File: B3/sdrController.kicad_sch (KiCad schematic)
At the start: 5 parts, among them U314 74HC32, U316 74HC00, U317 74HC74, U318 74HC08, U319 74HC32

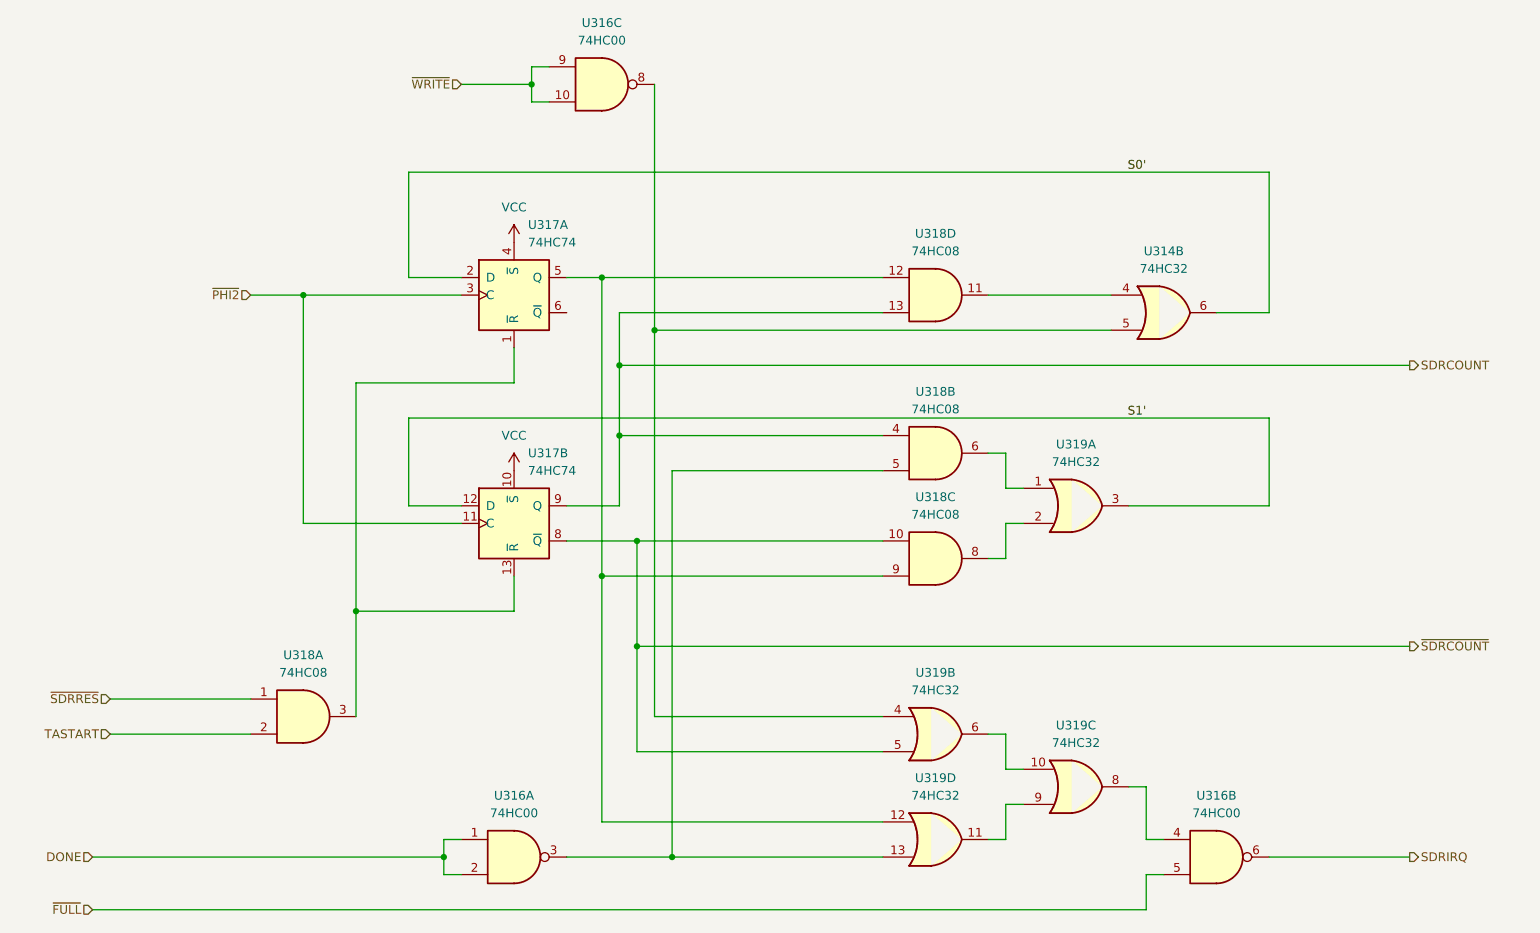
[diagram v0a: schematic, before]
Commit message: B3 added. First revision
Still not verified.
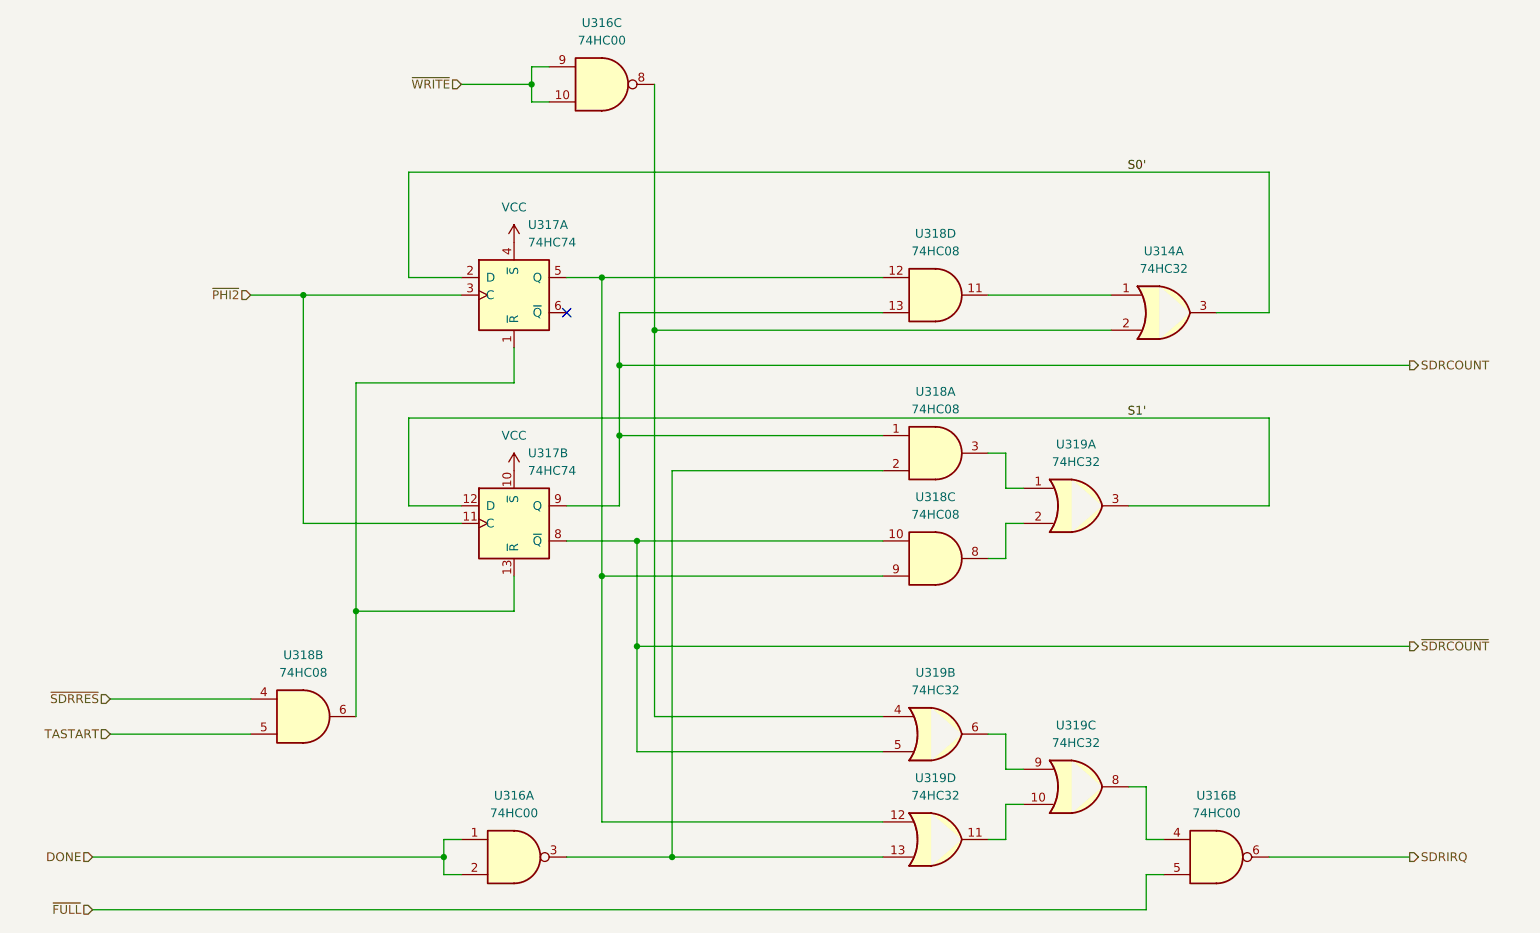
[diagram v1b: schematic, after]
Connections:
- net S0': now also U314.3; no longer U314.6
- net SDRCOUNT: now also U318.1; no longer U318.4
- net TASTART: now also U318.5; no longer U318.2
- net ~{SDRRES}: now also U318.4; no longer U318.1
- net at U318.11: now also U314.1; no longer U314.4
- net at U319.11: now also U319.10; no longer U319.9
- net at U316.3, U319.13: now also U318.2; no longer U318.5
- net at U316.8, U319.4: now also U314.2; no longer U314.5
- net at U319.6: now also U319.9; no longer U319.10
- net at U317.1 (~{R}), U317.13 (~{R}): now also U318.6; no longer U318.3
- net at U319.1: now also U318.3; no longer U318.6
- no-connect marks 0 -> 1
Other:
- moved on the sheet: U318A, U318B

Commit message: .
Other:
- company: (none) -> Daniel Molina
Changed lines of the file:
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@@
   (title_block
     (title "74HCT6526 Board 3")
-    (date "2022-09-11")
-    (rev "0.1")
+    (date "2022-10-08")
+    (rev "0.1.2")
+    (company "Daniel Molina")
+    (comment 1 "https://github.com/dmolinagarcia/74HCT6526")
   )
   (junction (at 127 68.58) (diameter 0) (color 0 0 0 0)

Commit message: .
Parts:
- added unit 4 of U316
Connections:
- net SDRIRQ: no longer names the net of U316.6
- net SDRIRQ: now also U316.12, U316.13
- new net ~{SDRIRQ}: U316.11
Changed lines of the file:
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@@
   (junction (at 127 68.58) (diameter 0) (color 0 0 0 0)
+  )
+  (junction (at 224.79 152.4) (diameter 0) (color 0 0 0 0)
   )
   (junction (at 137.16 152.4) (diameter 0) (color 0 0 0 0)
@@
     (stroke (width 0) (type default) (color 0 0 0 0))
   )
-  (wire (pts (xy 223.52 152.4) (xy 243.84 152.4))
-    (stroke (width 0) (type default) (color 0 0 0 0))
-  )
   (wire (pts (xy 182.88 109.22) (xy 185.42 109.22))
     (stroke (width 0) (type default) (color 0 0 0 0))
@@
     (stroke (width 0) (type default) (color 0 0 0 0))
   )
+  (wire (pts (xy 224.79 152.4) (xy 224.79 154.94))
+    (stroke (width 0) (type default) (color 0 0 0 0))
+  )
   (wire (pts (xy 91.44 116.84) (xy 114.3 116.84))
     (stroke (width 0) (type default) (color 0 0 0 0))
@@
     (stroke (width 0) (type default) (color 0 0 0 0))
   )
+  (wire (pts (xy 240.03 152.4) (xy 243.84 152.4))
+    (stroke (width 0) (type default) (color 0 0 0 0))
+  )
+  (wire (pts (xy 224.79 152.4) (xy 224.79 149.86))
+    (stroke (width 0) (type default) (color 0 0 0 0))
+  )
   (wire (pts (xy 116.84 40.64) (xy 116.84 38.1))
     (stroke (width 0) (type default) (color 0 0 0 0))
@@
   )
   (wire (pts (xy 83.82 71.12) (xy 106.68 71.12))
+    (stroke (width 0) (type default) (color 0 0 0 0))
+  )
+  (wire (pts (xy 223.52 152.4) (xy 224.79 152.4))
     (stroke (width 0) (type default) (color 0 0 0 0))
   )
@@
     (effects (font (size 1.27 1.27)) (justify right))
   )
-  (hierarchical_label "SDRIRQ" (shape output) (at 243.84 152.4 0)
+  (hierarchical_label "~{SDRIRQ}" (shape output) (at 243.84 152.4 0)
     (effects (font (size 1.27 1.27)) (justify left))
   )
@@
     (effects (font (size 1.27 1.27)) (justify right))
   )
+  (symbol (lib_id "74xx:74HC00") (at 232.41 152.4 0) (unit 4)
+    (in_bom yes) (on_board yes) (fields_autoplaced)
+    (property "Reference" "U316" (id 0) (at 232.41 143.51 0))
+    (property "Value" "74HC00" (id 1) (at 232.41 146.05 0))
+    (property "Footprint" "Package_SO:SO-14_3.9x8.65mm_P1.27mm" (id 2) (at 232.41 152.4 0)
+      (effects (font (size 1.27 1.27)) hide)
+    )
+    (property "Datasheet" "http://www.ti.com/lit/gpn/sn74hc00" (id 3) (at 232.41 152.4 0)
+      (effects (font (size 1.27 1.27)) hide)
+    )
+    (pin "1")
+    (pin "2")
+    (pin "3")
+    (pin "4")
+    (pin "5")
+    (pin "6")
+    (pin "10")
+    (pin "8")
+    (pin "9")
+    (pin "11")
+    (pin "12")
+    (pin "13")
+    (pin "14")
+    (pin "7")
+  )
   (symbol (lib_id "Custom 74xx:74HC08") (at 175.26 71.12 0) (unit 4)
